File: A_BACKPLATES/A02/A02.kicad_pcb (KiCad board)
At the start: 2 copper layers, 183 x 110 mm, 203 parts, among them J0 Conn_01x01_Male, J1 Conn_01x01_Male, J2 Conn_01x01_Male, J3 Conn_01x01_Male

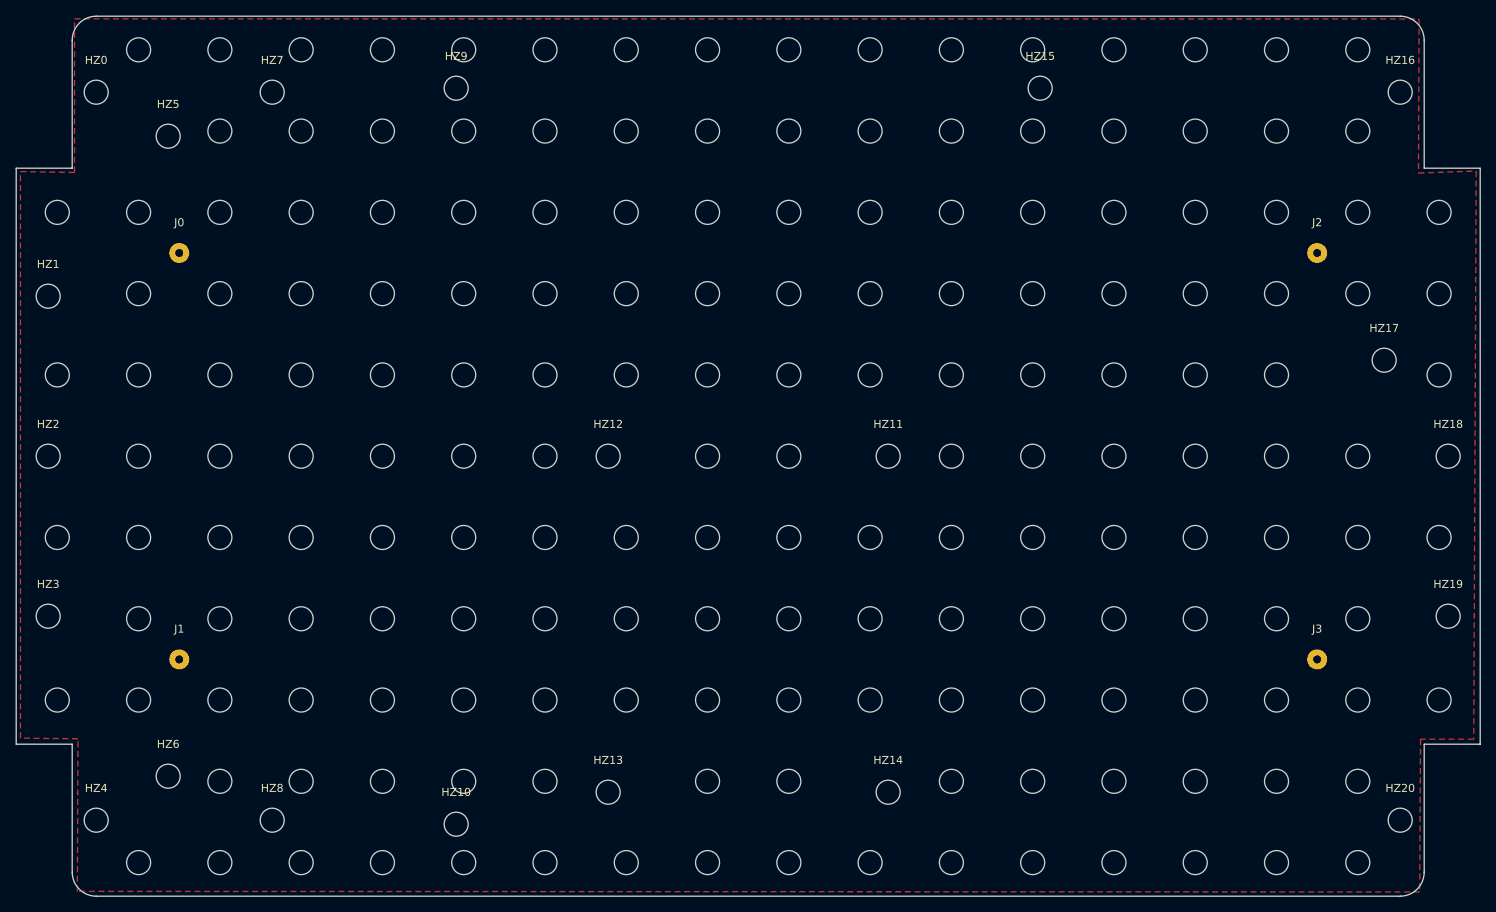
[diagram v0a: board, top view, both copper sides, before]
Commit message: oshw logo and silks added
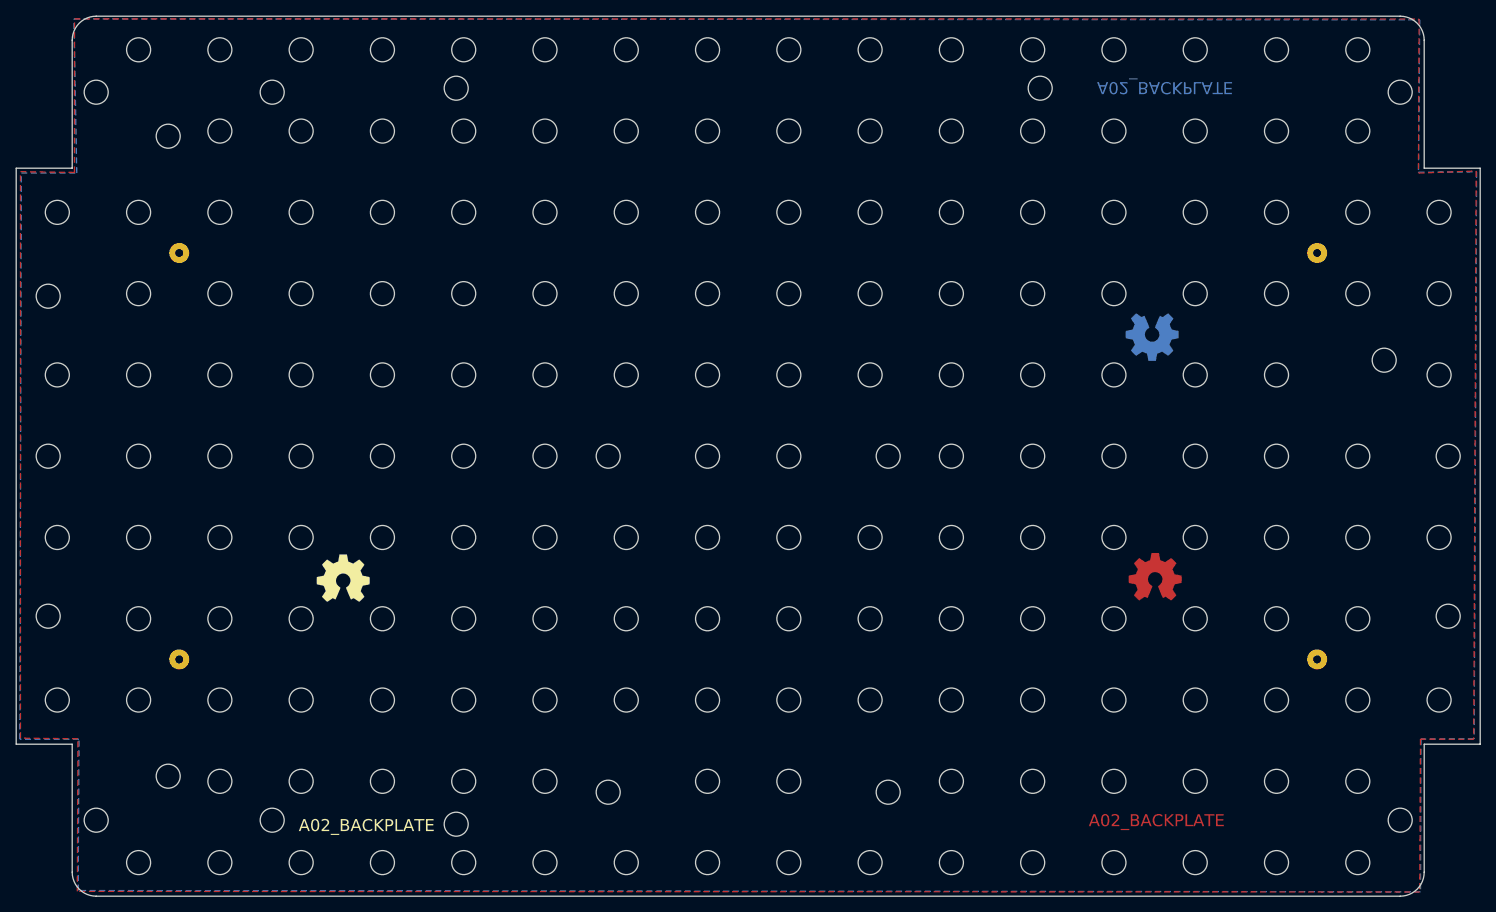
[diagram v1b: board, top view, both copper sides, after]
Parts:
- added REF**: OSHW-Symbol_6.7x6mm_Copper, Symbol:OSHW-Symbol_6.7x6mm_Copper, B.Cu at (160.7, 59.7)
- added REF**: OSHW-Symbol_6.7x6mm_SilkScreen, Symbol:OSHW-Symbol_6.7x6mm_SilkScreen, B.Cu at (59.1, 59.8)
- added REF**: OSHW-Symbol_6.7x6mm_Copper, Symbol:OSHW-Symbol_6.7x6mm_Copper, F.Cu at (161.0, 89.7)
- added REF**: OSHW-Symbol_6.7x6mm_SilkScreen, Symbol:OSHW-Symbol_6.7x6mm_SilkScreen, F.Cu at (59.5, 89.9)
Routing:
- added copper zone on B.Cu, net Net-(J0-Pad1)
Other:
- board text added: "A02_BACKPLATE"
